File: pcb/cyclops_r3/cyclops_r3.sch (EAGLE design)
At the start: 50 parts, among them IC1 317TO263, IC2 317, IC3 REF02Z, IC5 LM324D, Q1 2N5087

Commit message: Started designing the circuit.
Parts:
- removed GND1, V_IN1: BANANA_TO_BOARD, HOSS:BANANA_TO_BOARD
- removed MECH1, MECH2, MECH3, POW1: (no value), jumper:JP2Q
- removed POW2: SCREW2, HOSS:SCREW2
- removed Q1: 2N5087, transistor-pnp:2N5087
- removed Q2: (no value), transistor-power:PMOSFET_PTO220BH
- removed R1, R5, R6: 1.5k, HOSS:R-US_0207/7
- removed U$1: FUSE >2A, HOSS:NXT-FUSE
- removed U$3: SCREW2, cyclops:SCREW2
- added C1: 10uF, cyclops:C_0805
- added C10, C13: 1uF, cyclops:C-POL_1206
- added C11: 10uF, cyclops:C-POL_1206
- added C12: 47uF, cyclops:C-POL_0807
- added C8: 0.1uF, cyclops:C_0805
- added D1, D2: S1B-13-F, cyclops:DIODE-RECTS1B-13-F
- added DAC: MCP4921SOIC, cyclops:MCP4921SOIC
- added POWER: SCREW2, cyclops:SCREW2
- added R11: 240k, cyclops:R_0603
- added R7: 1.8k, cyclops:R_0603
- added S1: 219-04, cyclops:219-04
- C9: value 10u -> 1uF; device rcl:C-EU025-024X044 -> cyclops:C_0603
- IC1: value 317TO263 -> 317-N; device cyclops:317TO263 -> cyclops:317_TO263
- U$2: device adafruit:ARDUINO_R3_ICSP -> cyclops:ARDUINO_R3_ICSP
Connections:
- removed net N$21: U$2.5V$1
- removed net N$25: U$2.MISO
- removed net N$26: U$2.SCK
- removed net N$30: Q1.C, Q2.G, R1.1, R5.2
- removed net N$31: Q1.B, Q2.S, R6.1
- removed net N$61: POW1.1, U$1.P$1, U$1.P$2
- removed net N$66: U$2.MOSI
- removed net N$67: U$2.RST
- removed net N$68: U$2.GND$3
- removed net N$70: IC1.VI, U$3.P$1
- removed net P_SUP_BEFORE: Q1.E, R1.2, R6.2, U$1.P$3, U$1.P$4
- new net +12V: C12.+, C13.+, D1.A, D2.C, IC1.VO, R11.2
- new net +15V: C10.+, D1.C, IC1.VI, POWER.1
- new net +5V: C8.1, C9.1, DAC.VDD, U$2.5V$1
- new net CS: DAC.#CS, S1.1, S1.2, S1.3, S1.4
- new net CS0: S1.8, U$2.D1
- new net CS1: S1.7, U$2.D2
- new net CS2: S1.6, U$2.D3
- new net CS3: S1.5, U$2.D4
- new net DACA: DAC.DACA
- new net LDAC: DAC.LDAC, U$2.D0
- new net N$72: C11.+, D2.A, IC1.ADJ, R11.1, R7.2
- new net REFA: C1.1, DAC.REFA
- new net SCLK: DAC.SCK, U$2.SCK
- new net SDI: DAC.SDI, U$2.MOSI
- net GND: now also C1.2, C10.-, C11.-, C12.-, C13.-, C8.2, C9.2, DAC.AVSS, POWER.2, R7.1, U$2.GND$3; no longer C9.1, GND1.P$1, POW1.4, POW2.P$1, R5.1
- net P_SUP: no longer C9.2, Q2.D

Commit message: More work on the circuit schematic.
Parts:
- removed +12V, GND2: BANANA_TO_BOARD, HOSS:BANANA_TO_BOARD
- removed C6: 0.1uF, rcl:C-EU050-024X044
- removed IC2: 317, HOSS:317
- removed IC3: REF02Z, linear:REF02Z
- removed IMEAS_K: 10k, HOSS:TRIM_US-RJ6S
- removed JP1: (no value), jumper:JP3Q
- removed ON: (no value), led:LED3MM
- removed R10: 240, HOSS:R-US_0207/7
- removed REG_ADJ: 5k, HOSS:TRIM_US-RJ6S
- removed R_CURR: 0.2, HOSS:R-US_
- added C14: ??, cyclops:C_0603
- added R1: ??, cyclops:R_0603
- added R5: 1k 0.1%, cyclops:R_0603
- added R6: 0.2, cyclops:R_2512
- added U1: ADR03AKSZ-REEL7, cyclops:ADR03AKSZ-REEL7
- C4: value 0.1uF -> 1uF; device rcl:C-EU050-024X044 -> cyclops:C_0805
- C5: value 1.0uF -> 0.1uF; device rcl:C-EU025-024X044 -> cyclops:C_0603
- C8: device cyclops:C_0805 -> cyclops:C_0603
- C9: device cyclops:C_0603 -> cyclops:C_0805
- IC5: device linear:LM324D -> cyclops:LM324D
- R12, R9: device HOSS:R-US_0207/7 -> cyclops:R_0603
- R2: value 1.5k -> 4k 0.1%; device HOSS:R-US_0207/7 -> cyclops:R_0603
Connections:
- removed net N$14: IC5C.+IN, JP1.2
- removed net N$17: JP1.5, JP1.6
- removed net N$18: JP1.3
- removed net N$24: R9.1, REF_ADJ.A
- removed net N$28: ON.A, R2.1
- removed net P_SUP: C4.1, IC2.VI
- new net TEMP: U1.TEMP
- net +12V: now also C4.1, C5.1, U1.VIN
- net CS0: now also S1.5, U$2.D0; no longer S1.8, U$2.D1
- net CS1: now also S1.6, U$2.D1; no longer S1.7, U$2.D2
- net CS2: now also S1.7, U$2.D2; no longer S1.6, U$2.D3
- net CS3: now also S1.8, U$2.D3; no longer S1.5, U$2.D4
- net DACA: now also C14.1, R1.2
- net GND: now also C14.2, R1.1, R5.2, R6.1, R9.1, U1.GND; no longer C6.2, GND2.P$1, IC3.GND, IMEAS_K.A, ON.C, R9.2, REG_ADJ.S, R_CURR.1
- net LDAC: now also U$2.D4; no longer U$2.D0
- net N$15: now also R2.1; no longer IMEAS_K.S
- net N$19: now also R9.2, REF_ADJ.E; no longer IC2.ADJ, R10.1, REG_ADJ.E
- net N$2: now also R6.2; no longer R_CURR.2
- net N$20: now also U1.TRIM; no longer IC3.TRM
- net N$4: now also R2.2, R5.1; no longer IMEAS_K.E
- net N$8: now also IC5C.+IN; no longer JP1.4
- net N$9: no longer IC5C.OUT, JP1.1
- net P_12V: no longer +12V.P$1, C5.1, C6.1, IC2.VO, IC3.V+, R10.2, R2.2
- net REFA: now also REF_ADJ.A, U1.VOUT
- net REF_5V: no longer IC3.VO, REF_ADJ.E

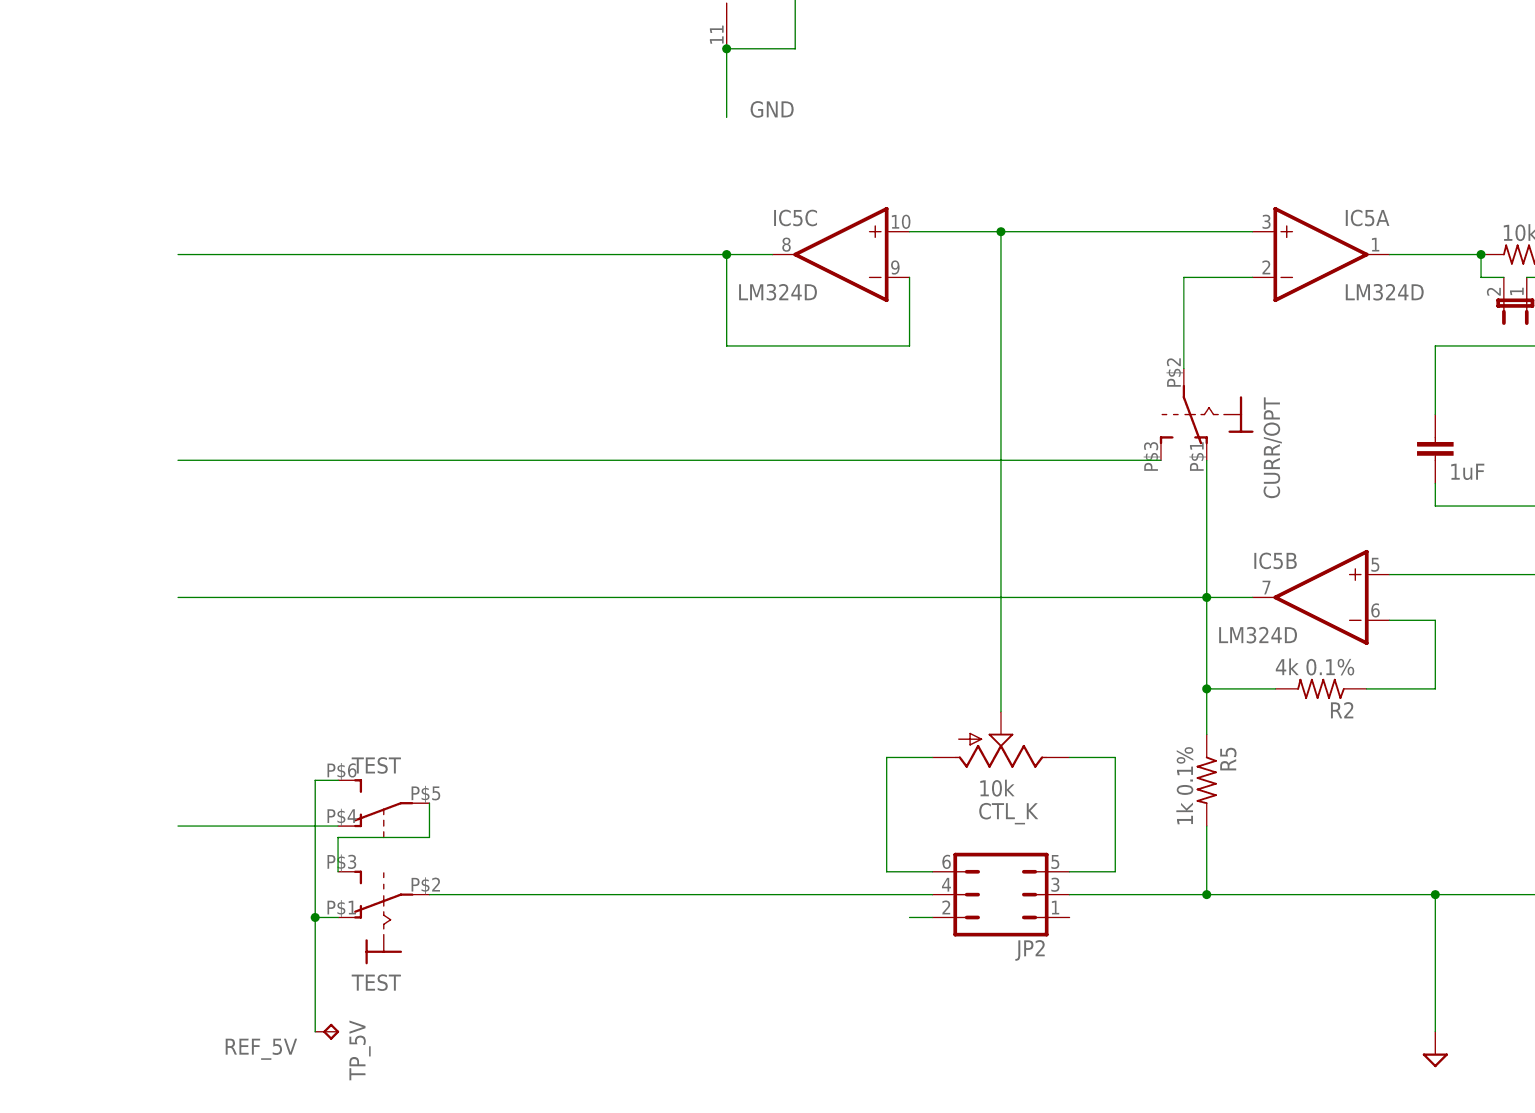
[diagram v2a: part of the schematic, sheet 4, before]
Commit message: Added reverse polarity protection to power input.
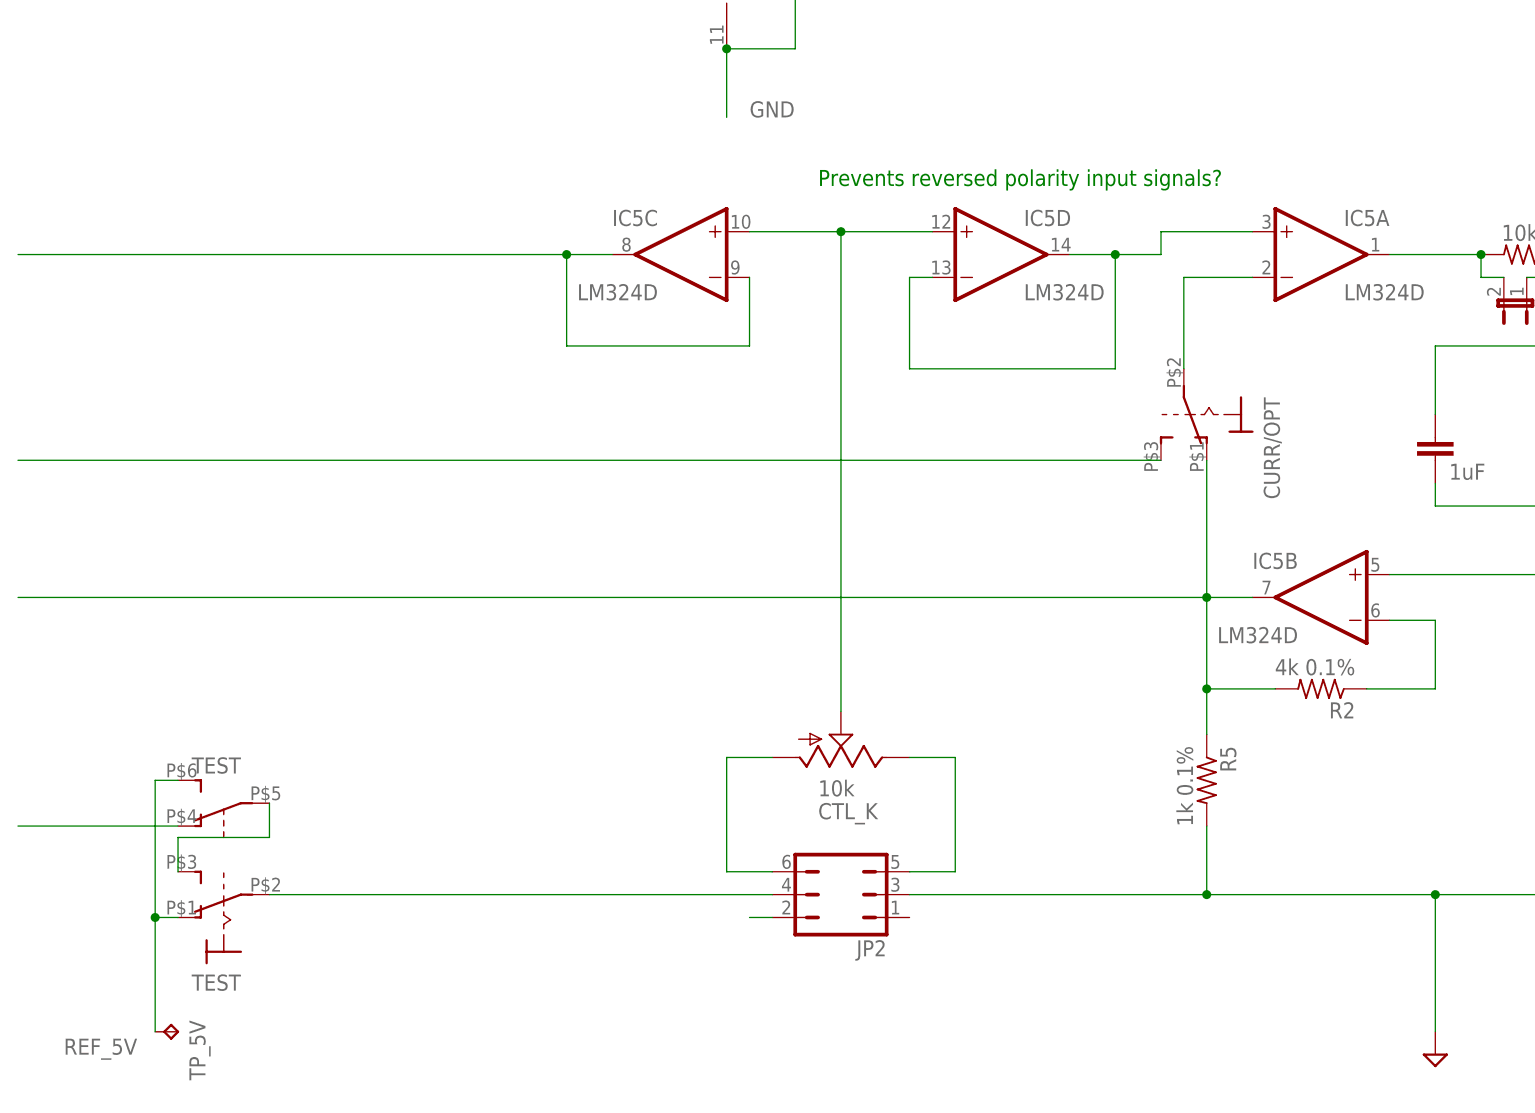
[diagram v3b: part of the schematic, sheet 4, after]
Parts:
- added D3: MMSZ5240B, cyclops:Z-DIODE_MMSZ
- added Q1: SUM11006, transistor-fet:IRF9530
- added R10: 10k, cyclops:R_0603
- REF_ADJ: device HOSS:TRIM_US-RJ6S -> cyclops:TRIM_US-SM-42/43W
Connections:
- new net N$14: IC5A.+IN, IC5D.-IN, IC5D.OUT
- new net N$17: POWER.1, Q1.D
- new net N$18: D3.A, Q1.G, R10.2
- net +15V: now also D3.C, Q1.S; no longer POWER.1
- net GND: now also R10.1
- net N$8: now also IC5D.+IN; no longer IC5A.+IN
- net N$9: now also IC5C.OUT
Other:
- note added: "Prevents reversed polarity input signals?"
- moved on the sheet: CTL_K, IC5C, JP2, POWER, TEST, TP_5V

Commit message: Some additions/changes to the schematic. All the power comonents should occupy the bottom of the board. The Heat sink will be on top. Ample via connected the two sides. Mica insert will be needed to insulate the heatsink.
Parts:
- removed C7: 0.1uF, rcl:C-EU050-024X044
- removed POWER: SCREW2, cyclops:SCREW2
- removed TEST: (no value), HOSS:SP3T_SWITCH
- removed TP_5V: TPPAD1-13, testpad:TPPAD1-13
- added I/O_BLOCK: SCREW8, cyclops:SCREW8
- Q1: device transistor-fet:IRF9530 -> cyclops:SUM110P06_TO-262
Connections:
- removed net N$23: TEST1.S, TESTB.P
- removed net P_12V: C7.1, IC5P.V+
- removed net REF_5V: TEST1.O, TESTB.S, TP_5V.TP
- new net BUFTEMP: I/O_BLOCK.8
- new net LED+: I/O_BLOCK.3
- new net LED-: I/O_BLOCK.4
- new net N$21: JP2.3, R5.2, R6.1
- new net VAUX: I/O_BLOCK.7
- new net VI: I/O_BLOCK.6
- new net VREF: I/O_BLOCK.5
- net GND: now also I/O_BLOCK.2; no longer C7.2, IC5P.V-, JP2.3, POWER.2, R5.2, R6.1
- net N$10: now also I/O_BLOCK.1; no longer TESTB.O
- net N$17: no longer POWER.1
- net N$6: no longer TEST1.P

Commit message: Added phase-reversal protection circuit to user supplied input pin (which used to go right to the noninverting pin of the LM324.
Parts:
- removed C2: 0.1uF, rcl:C-EU050-024X044
- removed C3: 1uF, rcl:C-EU025-024X044
- removed JP2: (no value), jumper:JP3Q
- removed JP3, JP4, JP5, JP6: (no value), jumper:JP1E
- removed R6: 0.2, cyclops:R_2512
- added C15, C17, C7: 1uF, cyclops:C_0805
- added C16, C18, C6: 0.1uF, cyclops:C_0603
- added D4, D5: 1N4148WS, cyclops:DIODESOD-323F
- added R13: 10k, cyclops:R_0603
- added RSENSE: 0.1, cyclops:R_2512
- added SJ1: (no value), jumper:SJ
- added U2: OP1177, cyclops:OP1177ARMZ
- DAC: value MCP4921SOIC -> MCP4921
- IC5: value LM324D -> LM324
- R12: value 470 -> 1k
- R2: value 4k 0.1% -> 9k 0.1%
- R3: value 10k -> 470; device HOSS:R-US_0207/7 -> cyclops:R_0603
- R4: value 10k -> 1k; device HOSS:R-US_0207/7 -> cyclops:R_0603
- R8: value 120 -> 1k; device HOSS:R-US_0207/7 -> cyclops:R_0603
- R9: value 1k -> 120
- U1: value ADR03AKSZ-REEL7 -> ADR03
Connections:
- net N$1 renamed VFB
- removed net N$12: CTL_K.A, JP2.6
- removed net N$13: C2.2, R8.2
- removed net N$14: IC5A.+IN, IC5D.-IN, IC5D.OUT
- removed net N$16: JP2.2
- removed net N$21: JP2.3, R5.2, R6.1
- removed net N$27: JP4.2, R3.1
- removed net N$29: JP3.1, JP5.1, JP6.2, R4.1
- removed net N$6: JP2.4
- removed net N$69: JP6.1
- removed net N$8: CTL_K.S, IC5C.+IN, IC5D.+IN
- removed net N$9: IC5C.-IN, IC5C.OUT
- new net VIN: CTL_K.A
- net +12V: now also C15.1, C16.1, C17.1, C18.1, IC5P.V+, R12.1, U2.V+
- net BUFTEMP: now also U2.-IN, U2.OUT
- net GND: now also C15.2, C16.2, C17.2, C18.2, C7.2, CTL_K.E, D4.C, IC5P.V-, R13.2, R5.2, RSENSE.1, U2.V-; no longer C3.2, JP4.1, R8.1
- net N$11: now also C6.1, C7.1, SJ1.2; no longer C2.1, C3.1, JP5.2, R3.2
- net N$19: no longer R9.2
- net N$2: now also RSENSE.2; no longer R6.2
- net N$20: now also R3.2; no longer R12.2
- net N$22: now also R3.1; no longer R12.1
- net N$3: now also SJ1.1; no longer JP3.2, R4.2
- net N$4: now also C6.2, R9.2; no longer CURR/OPT.O, IC5B.OUT, R2.2, R5.1
- net N$5: now also D4.A, R12.2, R8.2; no longer CURR/OPT.S
- net N$7: now also CTL_K.S, D5.A, R8.1; no longer CTL_K.E, JP2.5
- net TEMP: now also U2.+IN
- net VAUX: now also CURR/OPT.S
- net VI: now also CURR/OPT.O, IC5B.OUT, R2.2, R5.1
- net VREF: now also D5.C, IC5A.+IN, IC5C.+IN, IC5C.-IN, IC5C.OUT, R13.1
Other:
- note removed: "Prevents reversed polarity input signals?"
